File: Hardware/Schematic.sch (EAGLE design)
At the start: 64 parts, among them IC1 XC6220A331MR-G, IC2 BD5229G-TR, J1 SAMACSYS_PARTS_USB4110-GF-A, J2 FH34SRJ-24S-0.5SH_99_, J4 112A-TAAR-R03_ATTEND, Q1 20V/4.2A/52mΩ/1.4W, Q2 SI1308EDL-T1-GE3, Q3 20V/4.2A/52mΩ/1.4W, U1 ESP32_WROVER_SPARKFUN-IC-POWE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, U2 ESP32-C6-WROOM-1-N8, U3 ESP32_WROVER_BME680_BME680

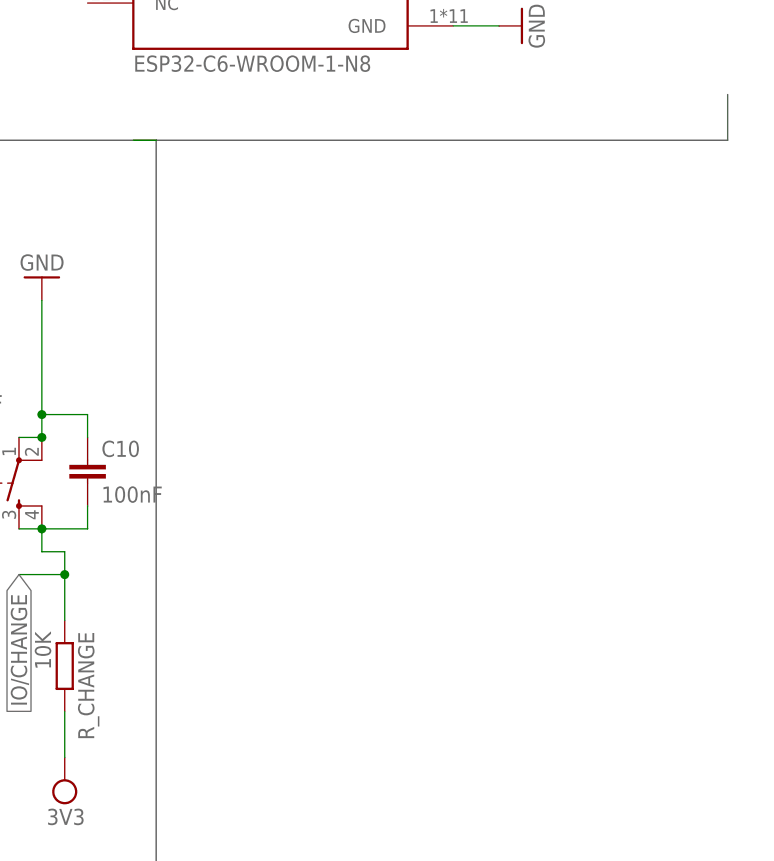
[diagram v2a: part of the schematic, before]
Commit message: add Battery Charge Level
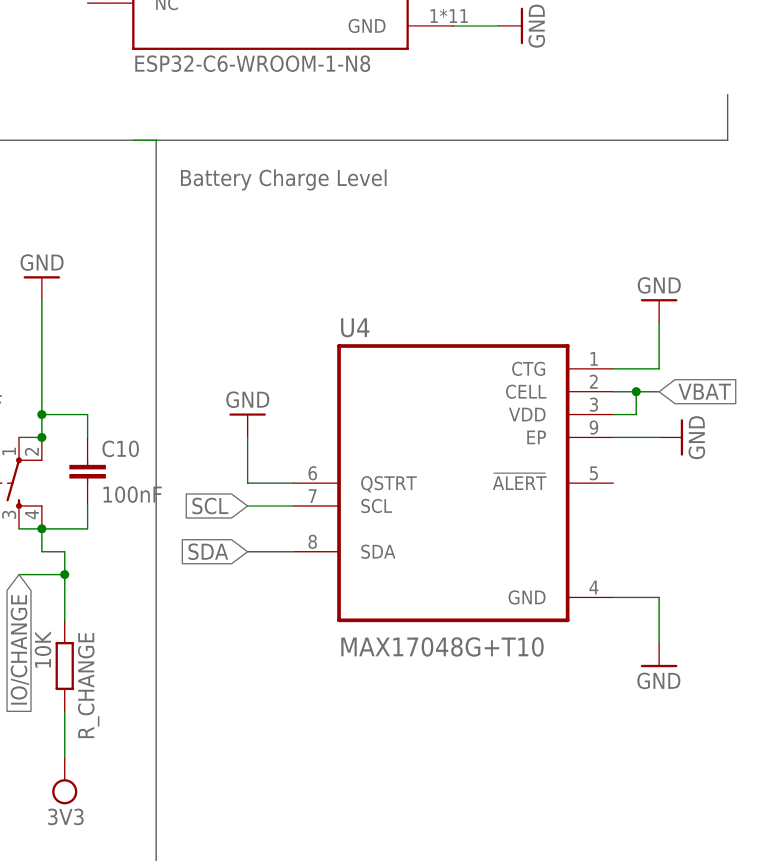
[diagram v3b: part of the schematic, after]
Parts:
- added U4: MAX17048G+T10, DeskAssistant v19 v1.flbr:MAX17048G+T10
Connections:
- net GND: now also U4.CTG, U4.EP, U4.GND, U4.QSTRT
- net SCL: now also U4.SCL
- net SDA: now also U4.SDA
- net VBAT: now also U4.CELL, U4.VDD
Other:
- note added: "Battery Charge Level"
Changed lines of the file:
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@@
 <part name="SUPPLY9" library="DeskAssistant v19 v1.flbr" library_urn="urn:adsk.wipprod:fs.file:vf.vVvdDOfaSfavM5thX5SjWw" deviceset="3V3-CIRCLE" device="" value="3V3"/>
 <part name="SUPPLY10" library="DeskAssistant v19 v1.flbr" library_urn="urn:adsk.wipprod:fs.file:vf.vVvdDOfaSfavM5thX5SjWw" deviceset="3V3-CIRCLE" device="" value="3V3"/>
+<part name="U4" library="DeskAssistant v19 v1.flbr" library_urn="urn:adsk.wipprod:fs.file:vf.vVvdDOfaSfavM5thX5SjWw" deviceset="MAX17048G+T10" device=""/>
+<part name="GND35" library="DeskAssistant v19 v1.flbr" library_urn="urn:adsk.wipprod:fs.file:vf.vVvdDOfaSfavM5thX5SjWw" deviceset="GND" device=""/>
+<part name="GND36" library="DeskAssistant v19 v1.flbr" library_urn="urn:adsk.wipprod:fs.file:vf.vVvdDOfaSfavM5thX5SjWw" deviceset="GND" device=""/>
+<part name="GND37" library="DeskAssistant v19 v1.flbr" library_urn="urn:adsk.wipprod:fs.file:vf.vVvdDOfaSfavM5thX5SjWw" deviceset="GND" device=""/>
+<part name="GND38" library="DeskAssistant v19 v1.flbr" library_urn="urn:adsk.wipprod:fs.file:vf.vVvdDOfaSfavM5thX5SjWw" deviceset="GND" device=""/>
 </parts>
 <sheets>
@@
 <text x="66.04" y="160.02" size="1.778" layer="95">Voltage Supervisor + Reset &amp;
 Boot / IO Button</text>
+<text x="157.48" y="162.56" size="1.778" layer="95">Battery Charge Level</text>
 </plain>
 <instances>
@@
 <instance part="SUPPLY10" gate="G$1" x="144.78" y="96.52" smashed="yes" rot="R180">
 <attribute name="VALUE" x="144.907" y="93.345" size="1.778" layer="96" rot="R180" align="bottom-center"/>
+</instance>
+<instance part="U4" gate="G$1" x="187.96" y="129.54" smashed="yes">
+<attribute name="NAME" x="175.26" y="145.78" size="2.0828" layer="95" ratio="10" rot="SR0"/>
+<attribute name="VALUE" x="175.26" y="110.3" size="2.0828" layer="96" ratio="10" rot="SR0"/>
+</instance>
+<instance part="GND35" gate="1" x="210.82" y="109.22" smashed="yes">
+<attribute name="VALUE" x="208.28" y="106.68" size="1.778" layer="96"/>
+</instance>
+<instance part="GND36" gate="1" x="213.36" y="134.62" smashed="yes" rot="R90">
+<attribute name="VALUE" x="215.9" y="132.08" size="1.778" layer="96" rot="R90"/>
+</instance>
+<instance part="GND37" gate="1" x="210.82" y="149.86" smashed="yes" rot="R180">
+<attribute name="VALUE" x="213.36" y="152.4" size="1.778" layer="96" rot="R180"/>
+</instance>
+<instance part="GND38" gate="1" x="165.1" y="137.16" smashed="yes" rot="R180">
+<attribute name="VALUE" x="167.64" y="139.7" size="1.778" layer="96" rot="R180"/>
 </instance>
 </instances>
@@
 <pinref part="GND34" gate="1" pin="GND"/>
 </segment>
+<segment>
+<pinref part="U4" gate="G$1" pin="CTG"/>
+<wire x1="205.74" y1="142.24" x2="210.82" y2="142.24" width="0.1524" layer="91"/>
+<wire x1="210.82" y1="142.24" x2="210.82" y2="147.32" width="0.1524" layer="91"/>
+<pinref part="GND37" gate="1" pin="GND"/>
+</segment>
+<segment>
+<pinref part="U4" gate="G$1" pin="EP"/>
+<wire x1="205.74" y1="134.62" x2="210.82" y2="134.62" width="0.1524" layer="91"/>
+<pinref part="GND36" gate="1" pin="GND"/>
+</segment>
+<segment>
+<pinref part="U4" gate="G$1" pin="GND"/>
+<wire x1="205.74" y1="116.84" x2="210.82" y2="116.84" width="0.1524" layer="91"/>
+<wire x1="210.82" y1="116.84" x2="210.82" y2="111.76" width="0.1524" layer="91"/>
+<pinref part="GND35" gate="1" pin="GND"/>
+</segment>
+<segment>
+<pinref part="U4" gate="G$1" pin="QSTRT"/>
+<wire x1="170.18" y1="129.54" x2="165.1" y2="129.54" width="0.1524" layer="91"/>
+<wire x1="165.1" y1="129.54" x2="165.1" y2="134.62" width="0.1524" layer="91"/>
+<pinref part="GND38" gate="1" pin="GND"/>
+</segment>
 </net>
 <net name="VUSB" class="0">
@@
 <wire x1="91.44" y1="185.42" x2="91.44" y2="203.2" width="0.1524" layer="91"/>
 <junction x="91.44" y="203.2"/>
+</segment>
+<segment>
+<pinref part="U4" gate="G$1" pin="CELL"/>
+<wire x1="205.74" y1="139.7" x2="208.28" y2="139.7" width="0.1524" layer="91"/>
+<wire x1="208.28" y1="139.7" x2="208.28" y2="137.16" width="0.1524" layer="91"/>
+<wire x1="208.28" y1="137.16" x2="205.74" y2="137.16" width="0.1524" layer="91"/>
+<pinref part="U4" gate="G$1" pin="VDD"/>
+<wire x1="208.28" y1="139.7" x2="210.82" y2="139.7" width="0.1524" layer="91"/>
+<junction x="208.28" y="139.7"/>
+<label x="210.82" y="139.7" size="1.778" layer="95" xref="yes"/>
 </segment>
 </net>
@@
 <label x="43.18" y="129.54" size="1.778" layer="95" rot="R180" xref="yes"/>
 </segment>
+<segment>
+<pinref part="U4" gate="G$1" pin="SDA"/>
+<wire x1="170.18" y1="121.92" x2="165.1" y2="121.92" width="0.1524" layer="91"/>
+<label x="165.1" y="121.92" size="1.778" layer="95" rot="R180" xref="yes"/>
+</segment>
 </net>
 <net name="SCL" class="0">
@@
 <label x="30.48" y="129.54" size="1.778" layer="95" rot="R180" xref="yes"/>
 </segment>
-</net>
+<segment>
+<pinref part="U4" gate="G$1" pin="SCL"/>
+<wire x1="170.18" y1="127" x2="165.1" y2="127" width="0.1524" layer="91"/>
+<label x="165.1" y="127" size="1.778" layer="95" rot="R180" xref="yes"/>
+</segment>
+</net>

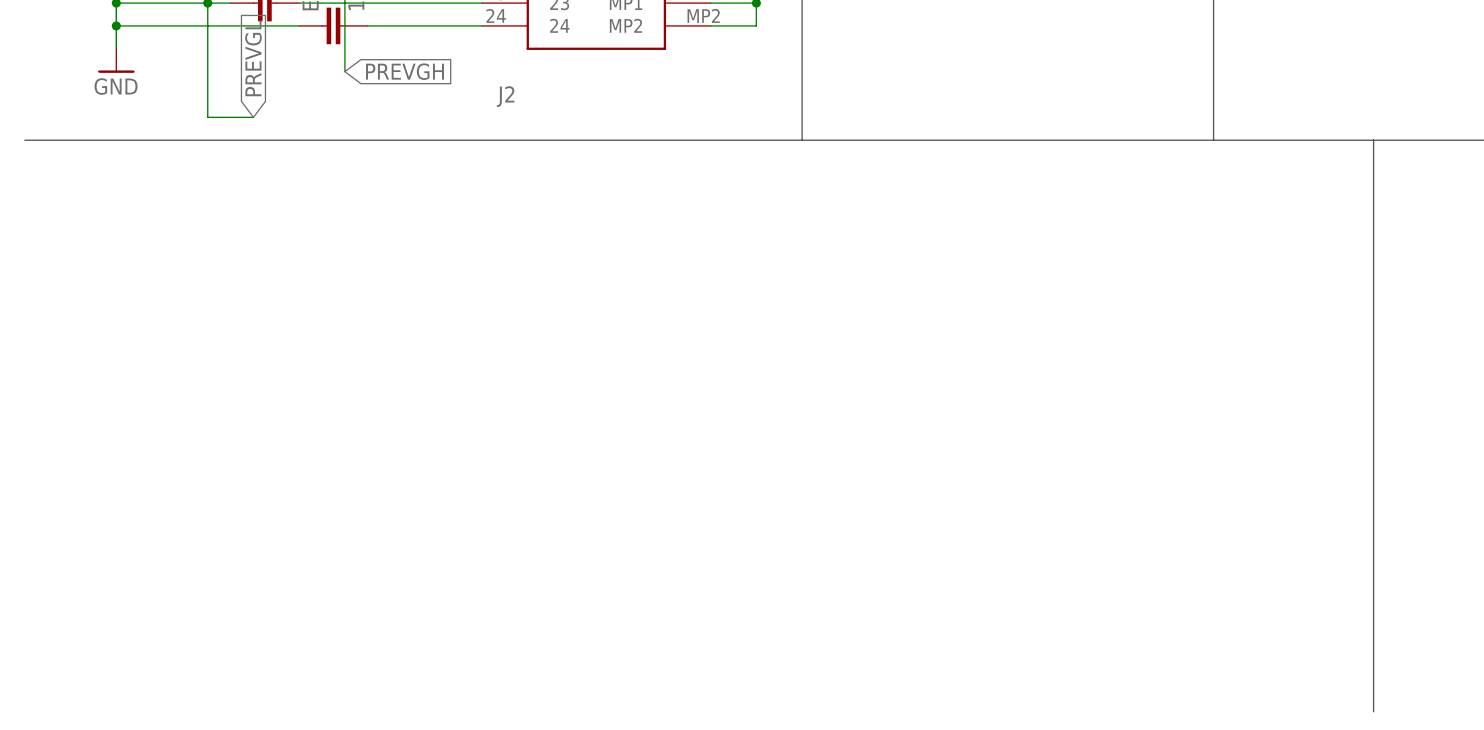
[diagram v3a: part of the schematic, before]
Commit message: add  RTC Module DS3231SN
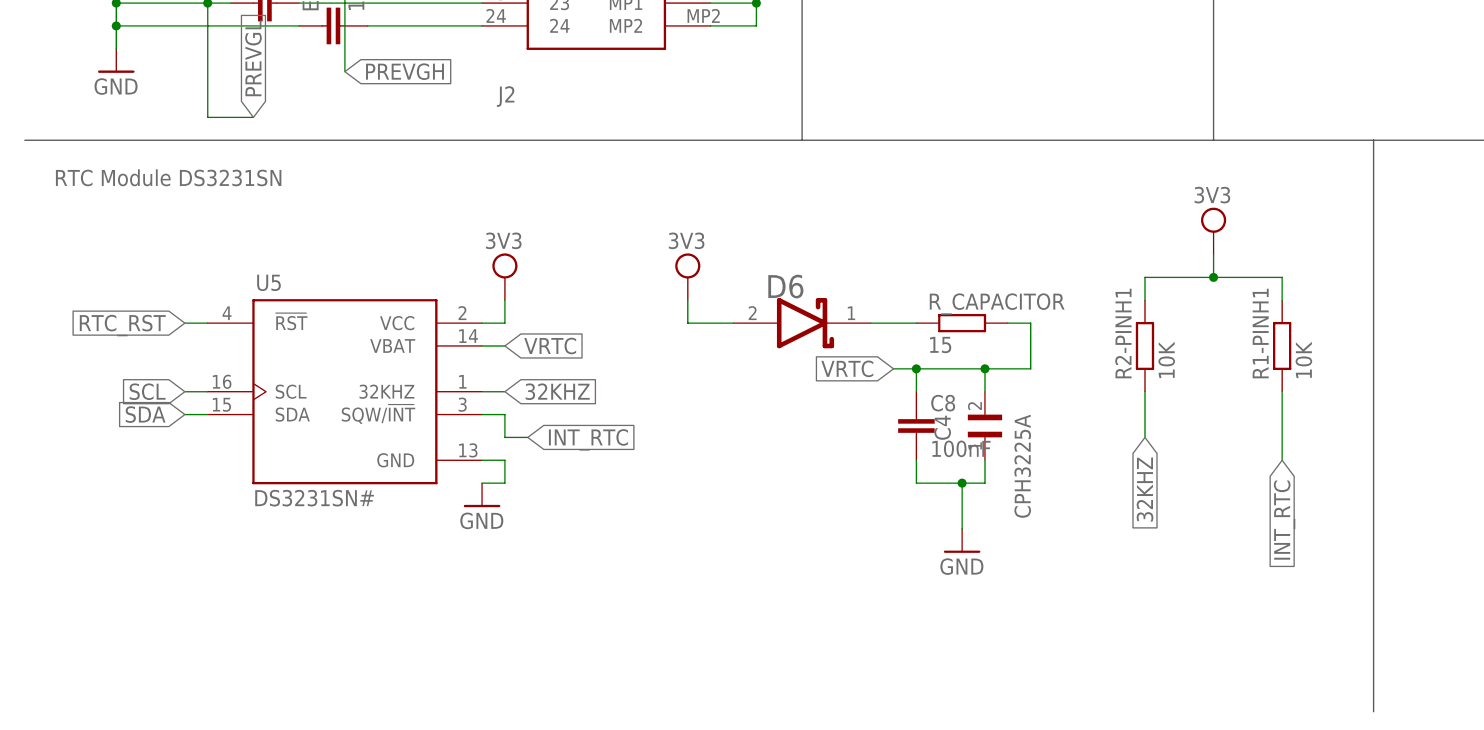
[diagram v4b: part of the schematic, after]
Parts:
- added C4: CPH3225A, DeskAssistant v19 v1.flbr:CPH3225A
- added C8: 100nF, DeskAssistant v19 v1.flbr:ESP32_WROVER_EAGLE-LTSPICE_CC0402
- added D6: ESP32_WROVER_AVX---SD0805S020S1R0_AVX_SD0805S020S1R0_0_0AVX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, DeskAssistant v19 v1.flbr:ESP32_WROVER_AVX---SD0805S020S1R0_AVX_SD0805S020S1R0_0_0AVX_SD0805S020S1R0_0_0
- added R1-PINH1, R2-PINH1: 10K, DeskAssistant v19 v1.flbr:ESP32_WROVER_EAGLE-LTSPICE_RR0402
- added R_CAPACITOR: 15, DeskAssistant v19 v1.flbr:ESP32_WROVER_EAGLE-LTSPICE_RR0402
- added U5: DS3231SN#, DeskAssistant v19 v1.flbr:DS3231SN#
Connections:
- new net N$21: D6.CATHODE, R_CAPACITOR.1
- new net VRTC: C4.2, C8.1, R_CAPACITOR.2, U5.VBAT
- net 32KHZ: now also R2-PINH1.1, U5.32KHZ
- net 3V3: now also D6.ANODE, R1-PINH1.2, R2-PINH1.2, U5.VCC
- net GND: now also C4.1, C8.2, U5.GND
- net INT_RTC: now also R1-PINH1.1, U5.SQW/!INT
- net RTC_RST: now also U5.!RST
- net SCL: now also U5.SCL
- net SDA: now also U5.SDA
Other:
- note added: "RTC Module DS3231SN"

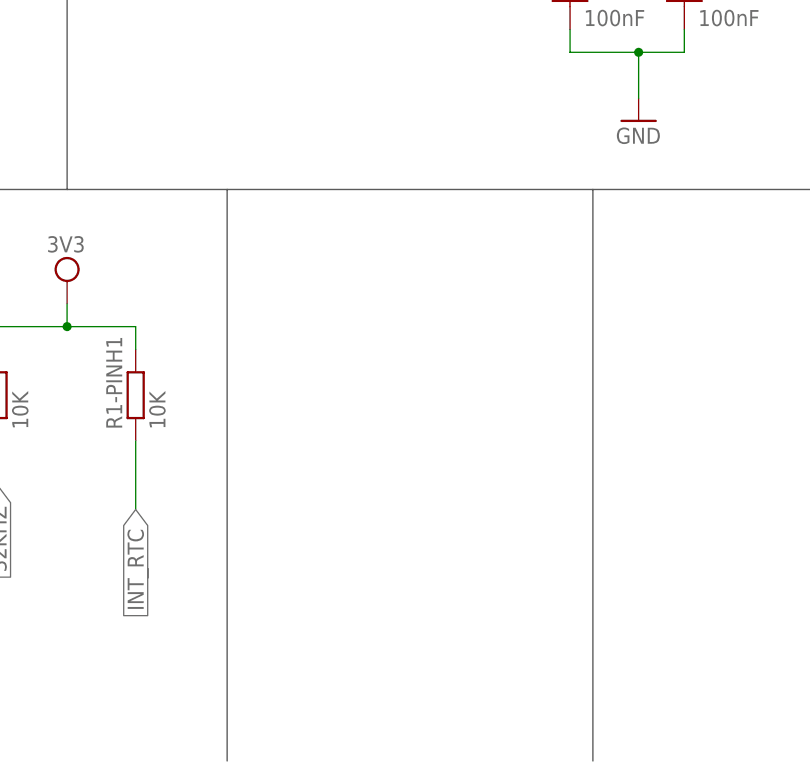
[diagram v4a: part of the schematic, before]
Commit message: add test pads
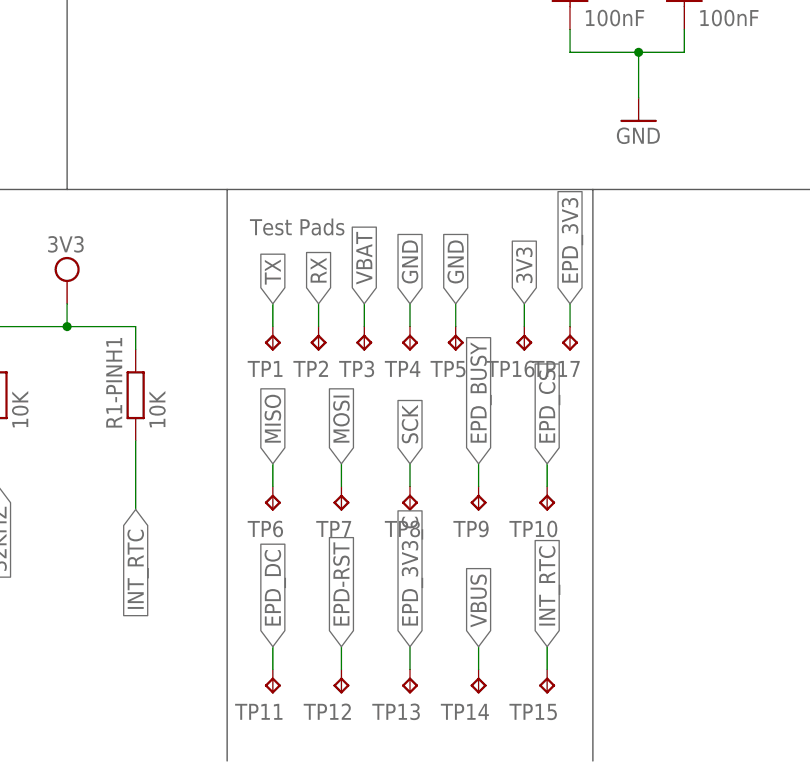
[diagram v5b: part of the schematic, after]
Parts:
- added TP1, TP10, TP11, TP12, TP13, TP14, TP15, TP16, TP17, TP2, TP3, TP4, TP5, TP6, TP7, TP8, TP9: TPTP20R, DeskAssistant v19 v1.flbr:TPTP20R
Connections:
- net 3V3: now also TP16.TP
- net EPD-RST: now also TP12.TP
- net EPD_3V3: now also TP17.TP
- net EPD_3V3_C: now also TP13.TP
- net EPD_BUSY: now also TP9.TP
- net EPD_CS: now also TP10.TP
- net EPD_DC: now also TP11.TP
- net GND: now also TP4.TP, TP5.TP
- net INT_RTC: now also TP15.TP
- net MISO: now also TP6.TP
- net MOSI: now also TP7.TP
- net RX: now also TP2.TP
- net SCK: now also TP8.TP
- net TX: now also TP1.TP
- net VBAT: now also TP3.TP
- net VBUS: now also TP14.TP
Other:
- note added: "Test Pads"
